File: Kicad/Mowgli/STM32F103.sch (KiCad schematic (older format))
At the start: 7 parts

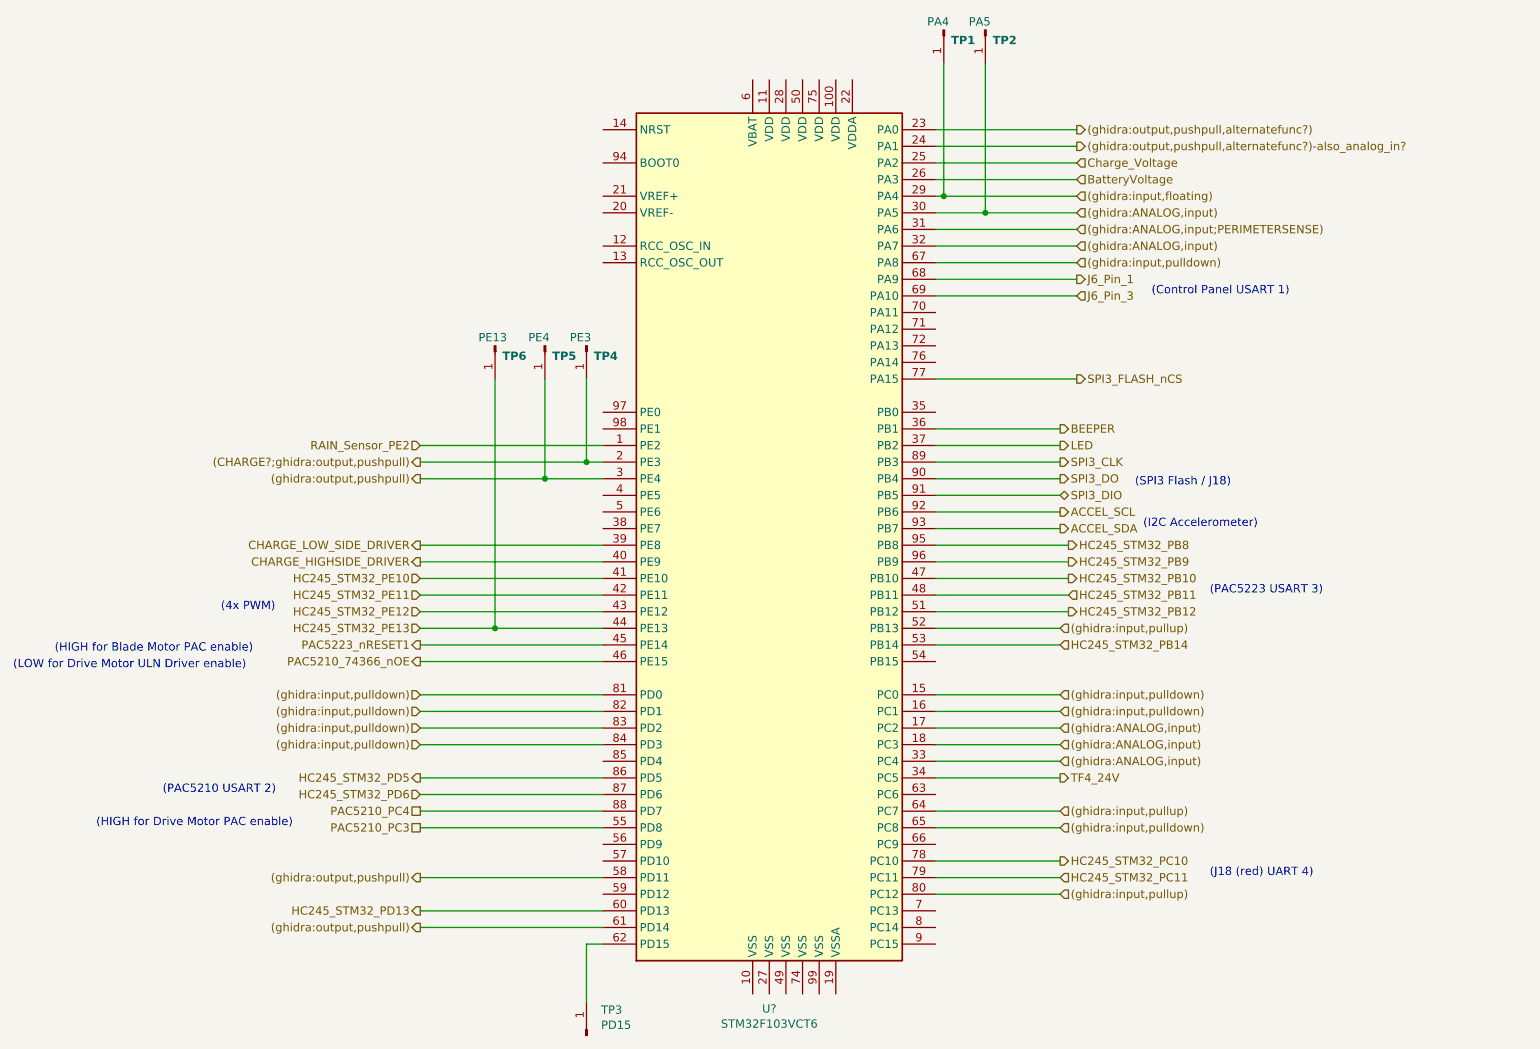
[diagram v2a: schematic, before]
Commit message: reversed mechanical tilt and accelerometer circuit
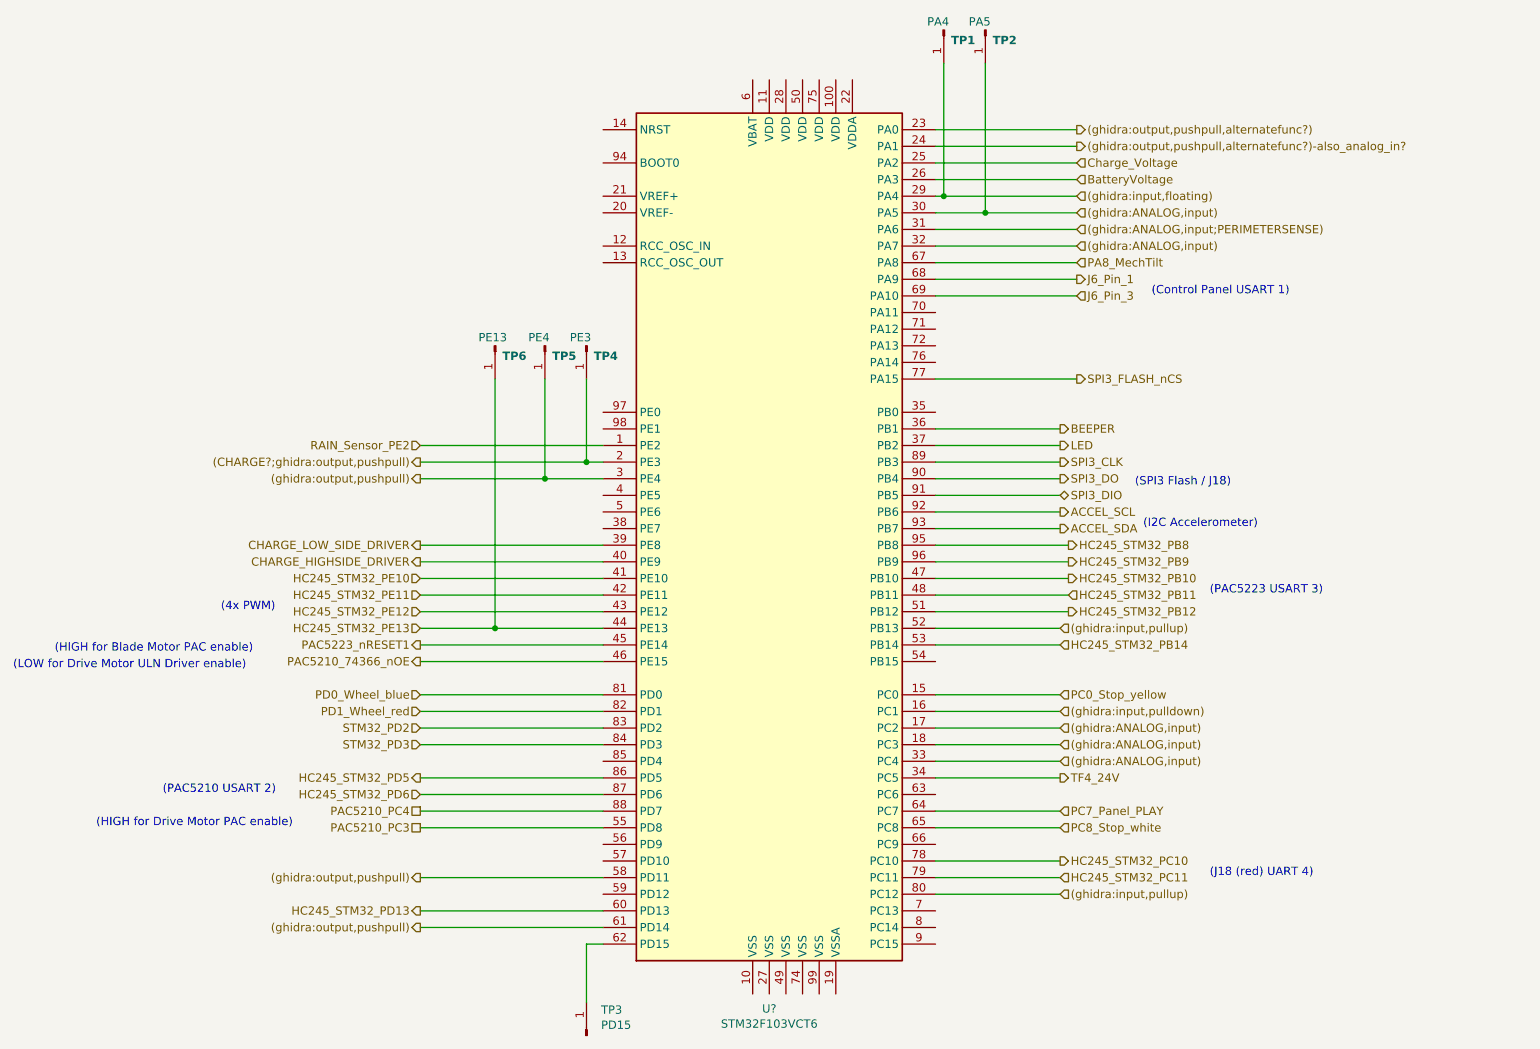
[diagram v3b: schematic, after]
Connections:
- net (ghidra:input,pulldown): no longer U?.15 (PC0), U?.65 (PC8), U?.67 (PA8), U?.81 (PD0), U?.82 (PD1), U?.83 (PD2), U?.84 (PD3)
- net (ghidra:input,pullup): no longer U?.64 (PC7)
- new net PA8_MechTilt: U?.67 (PA8)
- new net PC0_Stop_yellow: U?.15 (PC0)
- new net PC7_Panel_PLAY: U?.64 (PC7)
- new net PC8_Stop_white: U?.65 (PC8)
- new net PD0_Wheel_blue: U?.81 (PD0)
- new net PD1_Wheel_red: U?.82 (PD1)
- new net STM32_PD2: U?.83 (PD2)
- new net STM32_PD3: U?.84 (PD3)
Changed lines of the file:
@@
 $Descr A4 11693 8268
 encoding utf-8
-Sheet 3 14
+Sheet 14 14
 Title "Project Mowgli"
 Date "2022-05-22"
@@
 	7300 1700 6450 1700
 Text HLabel 7300 2200 2    50   Input ~ 0
-(ghidra:input,pulldown)
+PA8_MechTilt
 Wire Wire Line
 	7300 2200 6450 2200
 Text HLabel 3350 5000 0    50   Input ~ 0
-(ghidra:input,pulldown)
+STM32_PD2
 Text HLabel 3350 5100 0    50   Input ~ 0
-(ghidra:input,pulldown)
+STM32_PD3
 Text HLabel 3350 4900 0    50   Input ~ 0
-(ghidra:input,pulldown)
+PD1_Wheel_red
 Text HLabel 3350 4800 0    50   Input ~ 0
-(ghidra:input,pulldown)
+PD0_Wheel_blue
 Text HLabel 7300 1400 2    50   Output ~ 0
 (ghidra:output,pushpull,alternatefunc?)
@@
 	7200 4400 6450 4400
 Text HLabel 7200 5500 2    50   Input ~ 0
-(ghidra:input,pullup)
+PC7_Panel_PLAY
 Wire Wire Line
 	7200 5500 6450 5500
@@
 	7200 4900 6450 4900
 Text HLabel 7200 4800 2    50   Input ~ 0
-(ghidra:input,pulldown)
+PC0_Stop_yellow
 Wire Wire Line
 	7200 4800 6450 4800
 Text HLabel 7200 5600 2    50   Input ~ 0
-(ghidra:input,pulldown)
+PC8_Stop_white
 Wire Wire Line
 	7200 5600 6450 5600

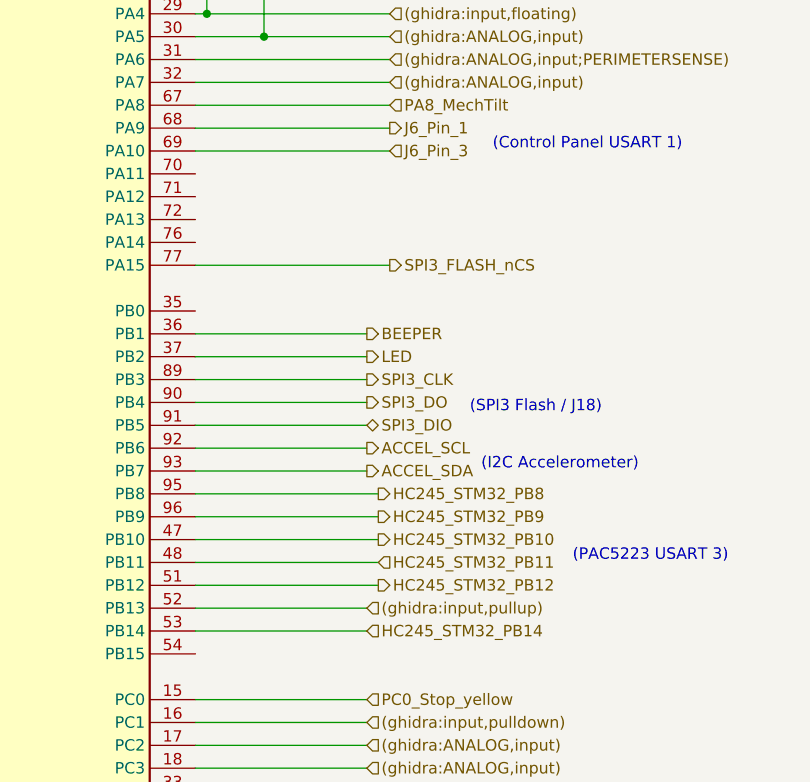
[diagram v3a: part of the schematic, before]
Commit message: added Panel Eliminator
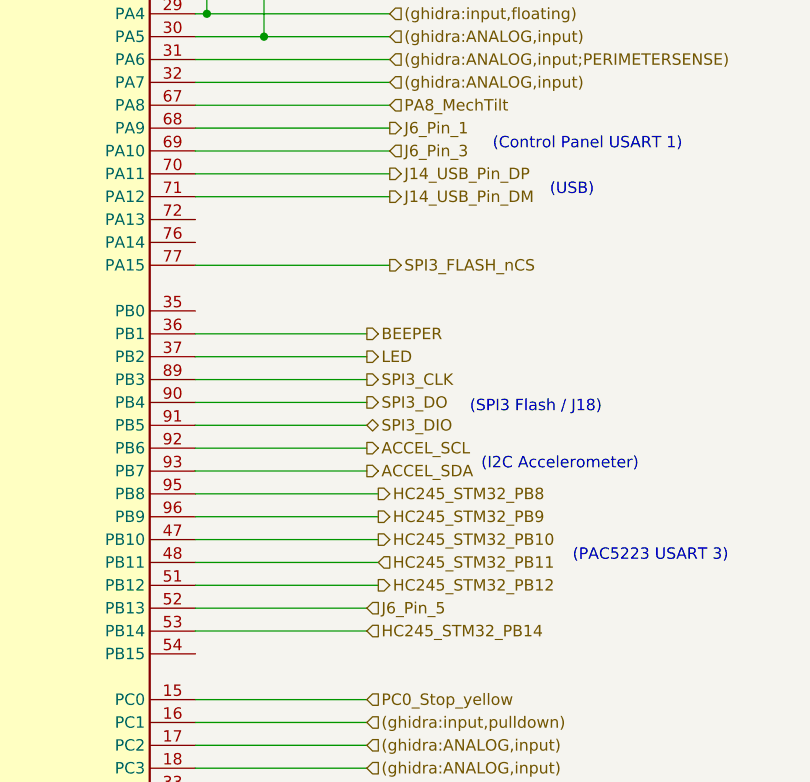
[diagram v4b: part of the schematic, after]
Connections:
- net (ghidra:input,pullup): no longer U?.52 (PB13)
- net J14_USB_Pin_DP: now reaches U?.70 (PA11)
- net J14_USB_Pin_DM: now reaches U?.71 (PA12)
- new net J6_Pin_5: U?.52 (PB13)
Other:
- note added: "(USB)"
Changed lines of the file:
@@
 	7200 5000 6450 5000
 Text HLabel 7200 4400 2    50   Input ~ 0
-(ghidra:input,pullup)
+J6_Pin_5
 Wire Wire Line
 	7200 4400 6450 4400
@@
 Wire Wire Line
 	3350 5900 4450 5900
+Text HLabel 7300 2500 2    50   Output ~ 0
+J14_USB_Pin_DP
+Text HLabel 7300 2600 2    50   Output ~ 0
+J14_USB_Pin_DM
+Wire Wire Line
+	7300 2600 6450 2600
+Wire Wire Line
+	6450 2500 7300 2500
+Text Notes 8000 2600 0    50   ~ 0
+(USB)
 $EndSCHEMATC

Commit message: kicad cleanup
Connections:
- net (ghidra:output,pushpull,alternatefunc?)-also_analog_in? renamed Charge_Current
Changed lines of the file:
@@
 (ghidra:output,pushpull,alternatefunc?)
 Text HLabel 7300 1500 2    50   Output ~ 0
-(ghidra:output,pushpull,alternatefunc?)-also_analog_in?
+Charge_Current
 Wire Wire Line
 	6450 1400 7300 1400

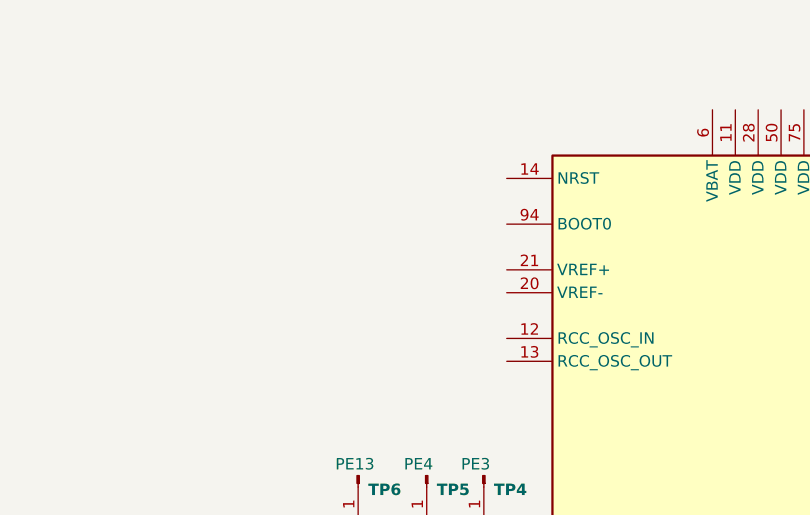
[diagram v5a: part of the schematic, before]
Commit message: kicad boot0 pin update
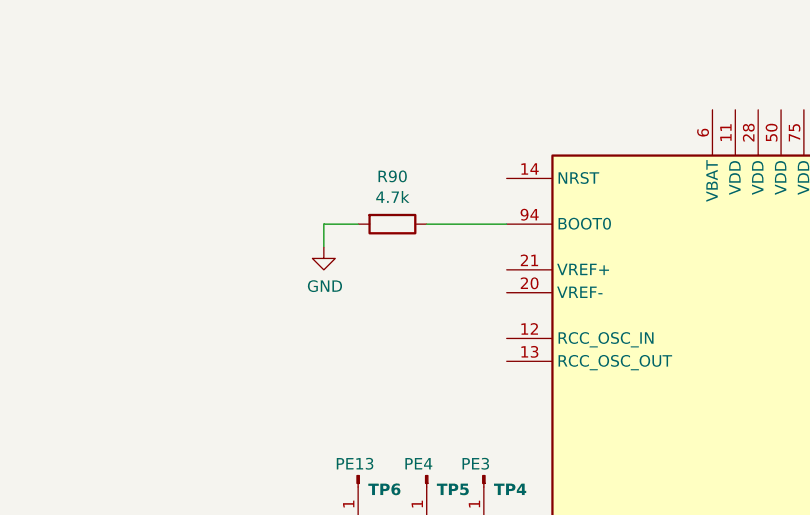
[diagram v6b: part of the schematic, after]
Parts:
- added R90: 4.7k, symbol Device:R
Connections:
- net at U?.94 (BOOT0): now also R90.1
- new net GND: R90.2
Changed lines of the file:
@@
 Text Notes 8000 2600 0    50   ~ 0
 (USB)
+$Comp
+L Device:R R90
+U 1 1 62D3794F
+P 3950 1600
+F 0 "R90" V 3743 1600 50  0000 C CNN
+F 1 "4.7k" V 3834 1600 50  0000 C CNN
+F 2 "" V 3880 1600 50  0001 C CNN
+F 3 "~" H 3950 1600 50  0001 C CNN
+	1    3950 1600
+	0    1    1    0
+$EndComp
+Wire Wire Line
+	4450 1600 4100 1600
+$Comp
+L power:GND #PWR?
+U 1 1 62D3B72F
+P 3650 1700
+F 0 "#PWR?" H 3650 1450 50  0001 C CNN
+F 1 "GND" H 3655 1527 50  0000 C CNN
+F 2 "" H 3650 1700 50  0001 C CNN
+F 3 "" H 3650 1700 50  0001 C CNN
+	1    3650 1700
+	1    0    0    -1
+$EndComp
+Wire Wire Line
+	3800 1600 3650 1600
+Wire Wire Line
+	3650 1600 3650 1700
 $EndSCHEMATC
